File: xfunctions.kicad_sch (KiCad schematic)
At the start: 0 parts

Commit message: 스키메틱 작성
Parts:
- added D0, D1, D10, D11, D12, D13, D14, D15, D2, D3, D4, D5, D6, D7, D8, D9: D_Small, Diode_SMD:D_SOD-323, symbol Device:D_Small
- added SW0, SW1, SW10, SW11, SW12, SW13, SW14, SW15, SW2, SW3, SW4, SW5, SW6, SW7, SW8, SW9: SW_Push, PCM_Switch_Keyboard_Hotswap_Kailh:SW_Hotswap_Kailh_MX_1.00u, symbol Switch:SW_Push
- added U1: ProMicroC, SparkFun-Board:ProMicroC, symbol SparkFun-Board:ProMicroC
- added U2: 74HC4051, Package_SO:SO-16_3.9x9.9mm_P1.27mm, symbol 74xx:74HC4051
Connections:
- new net: D1.2 (A), SW1.1
- new net: D5.2 (A), SW5.1
- new net: D3.2 (A), SW3.1
- new net: D15.2 (A), SW15.1
- new net: D14.2 (A), SW14.1
- new net: D13.2 (A), SW13.1
- new net: D4.2 (A), SW4.1
- new net: D9.2 (A), SW9.1
- new net: D0.2 (A), SW0.1
- new net: D7.2 (A), SW7.1
- new net: D8.2 (A), SW8.1
- new net: D11.2 (A), SW11.1
- new net: D10.2 (A), SW10.1
- new net: D12.2 (A), SW12.1
- new net: D2.2 (A), SW2.1
- new net: D6.2 (A), SW6.1
- new net COL_00: SW0.2, SW8.2, U2.13 (A0)
- new net COL_01: SW1.2, SW9.2, U2.14 (A1)
- new net COL_02: SW10.2, SW2.2, U2.15 (A2)
- new net COL_03: SW11.2, SW3.2, U2.12 (A3)
- new net COL_04: SW12.2, SW4.2, U2.1 (A4)
- new net COL_05: SW13.2, SW5.2, U2.5 (A5)
- new net COL_06: SW14.2, SW6.2, U2.2 (A6)
- new net COL_07: SW15.2, SW7.2, U2.4 (A7)
- new net GND: U1.23 (GND), U1.3 (GND), U1.4 (GND), U2.6 (~{E}), U2.7 (VEE), U2.8 (GND)
- new net MULIO_00: U1.12 (D9/A9), U2.3 (A)
- new net MULSEL_00: U1.13 (D10/A10), U2.11 (S0)
- new net MULSEL_01: U1.14 (D16), U2.10 (S1)
- new net MULSEL_02: U1.15 (D14), U2.9 (S2)
- new net ROW_00: D0.1 (K), D1.1 (K), D2.1 (K), D3.1 (K), D4.1 (K), D5.1 (K), D6.1 (K), D7.1 (K), U1.10 (D7)
- new net ROW_01: D10.1 (K), D11.1 (K), D12.1 (K), D13.1 (K), D14.1 (K), D15.1 (K), D8.1 (K), D9.1 (K), U1.11 (D8/A8)
- new net VCC: U1.21 (5V), U2.16 (VCC)
- no-connect marks 0 -> 14

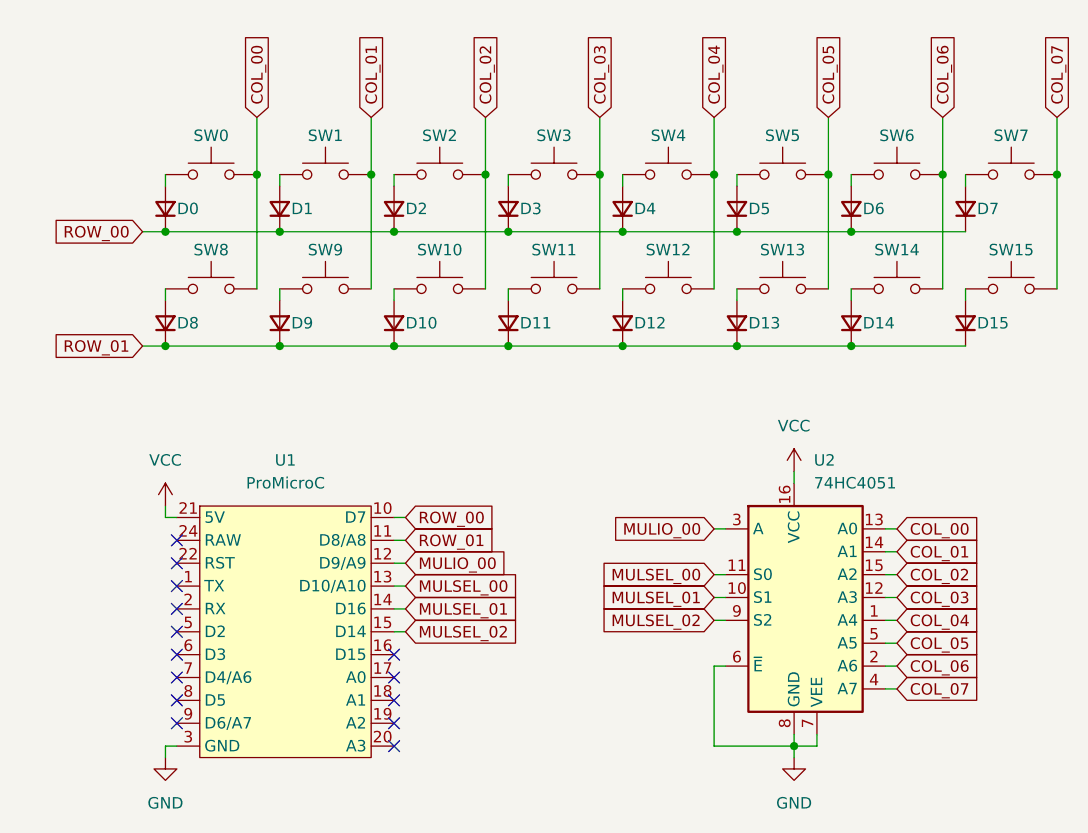
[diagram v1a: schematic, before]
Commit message: 스키메틱 수정
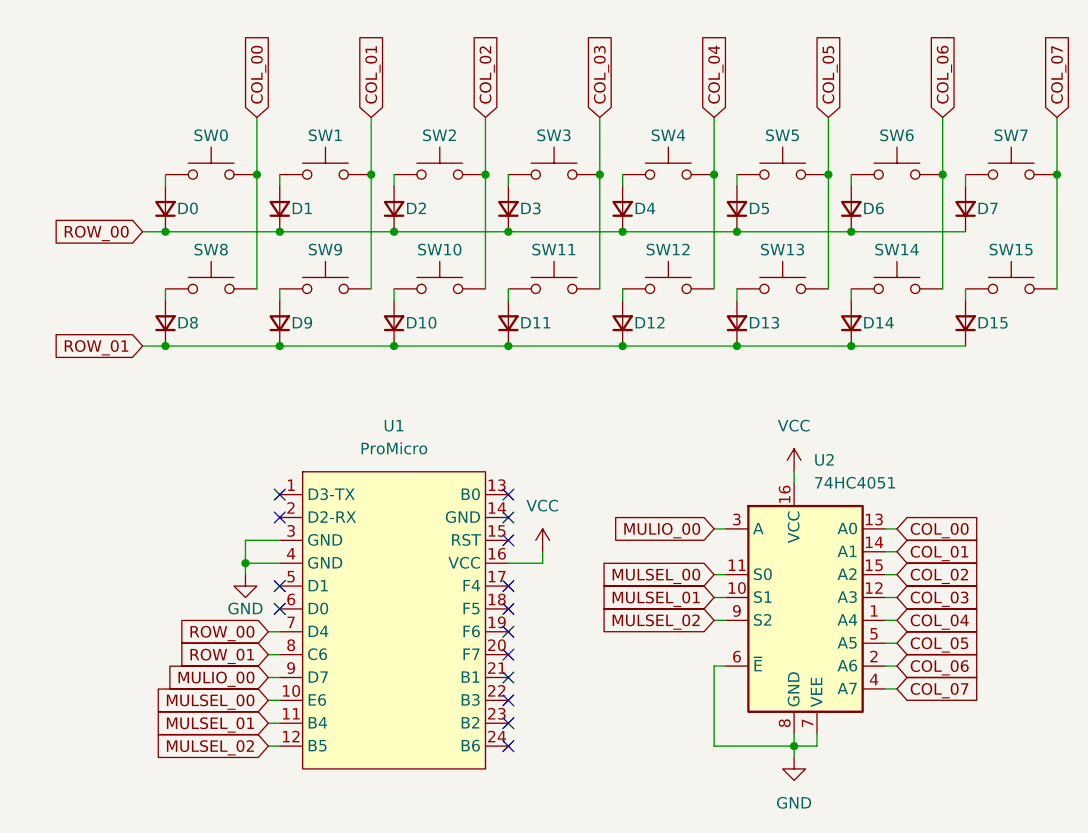
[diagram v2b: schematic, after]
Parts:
- removed U1: ProMicroC, SparkFun-Board:ProMicroC, symbol SparkFun-Board:ProMicroC
- added U1: ProMicro, PCM_marbastlib-xp-promicroish:ProMicro_USBup, symbol PCM_marbastlib-promicroish:Arduino_ProMicro
- SW0, SW1, SW10, SW11, SW12, SW13, SW14, SW15, SW2, SW3, SW4, SW5, SW6, SW7, SW8, SW9: footprint PCM_Switch_Keyboard_Hotswap_Kailh:SW_Hotswap_Kailh_MX_1.00u -> PCM_marbastlib-mx:SW_MX_HS_CPG151101S11_1u
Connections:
- net GND: now also U1.3 (GND), U1.4 (GND)
- net MULIO_00: now also U1.9 (D7)
- net MULSEL_00: now also U1.10 (E6)
- net MULSEL_01: now also U1.11 (B4)
- net MULSEL_02: now also U1.12 (B5)
- net ROW_00: now also U1.7 (D4)
- net ROW_01: now also U1.8 (C6)
- net VCC: now also U1.16 (VCC)
- no-connect marks 14 -> 15

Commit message: PCB 작성 완료
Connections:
- net COL_00: now also U2.5 (A5); no longer U2.13 (A0)
- net COL_01: now also U2.4 (A7); no longer U2.14 (A1)
- net COL_02: now also U2.2 (A6); no longer U2.15 (A2)
- net COL_03: now also U2.1 (A4); no longer U2.12 (A3)
- net COL_04: now also U2.15 (A2); no longer U2.1 (A4)
- net COL_05: now also U2.14 (A1); no longer U2.5 (A5)
- net COL_06: now also U2.13 (A0); no longer U2.2 (A6)
- net COL_07: now also U2.12 (A3); no longer U2.4 (A7)
- net MULIO_00: now also U1.17 (F4); no longer U1.9 (D7)
- net MULSEL_00: now also U1.7 (D4); no longer U1.10 (E6)
- net MULSEL_01: now also U1.8 (C6); no longer U1.11 (B4)
- net MULSEL_02: now also U1.9 (D7); no longer U1.12 (B5)
- net ROW_00: now also U1.5 (D1); no longer U1.7 (D4)
- net ROW_01: now also U1.12 (B5); no longer U1.8 (C6)
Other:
- moved on the sheet: U1
